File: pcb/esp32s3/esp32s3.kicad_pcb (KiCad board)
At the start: 2 copper layers, 64.5 x 64.5 mm, 82 parts, among them J1 USB_C_Receptacle_USB2.0_14P, J2 Battery, J3 GPS_ANT, Q1 DMG3414U, Q1_Xtal1 32.0MHz, SW1 BOOT, U1 ESP32-S3FN8, U2 AZ1117-3.3, U3 USBLC6-2SC6, U4 MCP73831-2-OT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

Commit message: pcb update!!!
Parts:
- added J4: LH128R-IG01, LH128R-IG01:LH128R-IG01, F.Cu at (159.7, 58.1)
- added Q2: DMG1012T, Package_TO_SOT_SMD:SOT-523, F.Cu at (157.4, 66.5)
- added R19: 10, Resistor_SMD:R_0402_1005Metric, F.Cu at (156.9, 60.0)
- added R20: 10K, Resistor_SMD:R_0402_1005Metric, F.Cu at (156.9, 61.9)
- added R21: 1K, Resistor_SMD:R_0402_1005Metric, F.Cu at (156.9, 63.9)
- C2: value 2p4 -> 2.4pF
- C4: value 2p7 -> 2.7pF
- C7, C8, C9: value 0.1uF -> 100nF
- L1: value 2n4 -> 2.4nH
- moved J1 14.9 mm to (129.5, 43.0), turned to 180 degrees
- moved U2 3.45 mm to (134.0, 62.0)
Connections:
- U1 pad 42: GP37 -> LCD_BL
- U1 pad 43: GP38 -> LCD_DC
- U1 pad 44: GP39 -> LCD_CS
- U1 pad 45: GP40 -> LCD_SCK
- U1 pad 47: GP41 -> LCD_SDA
- U1 pad 48: GP42 -> LCD_RST

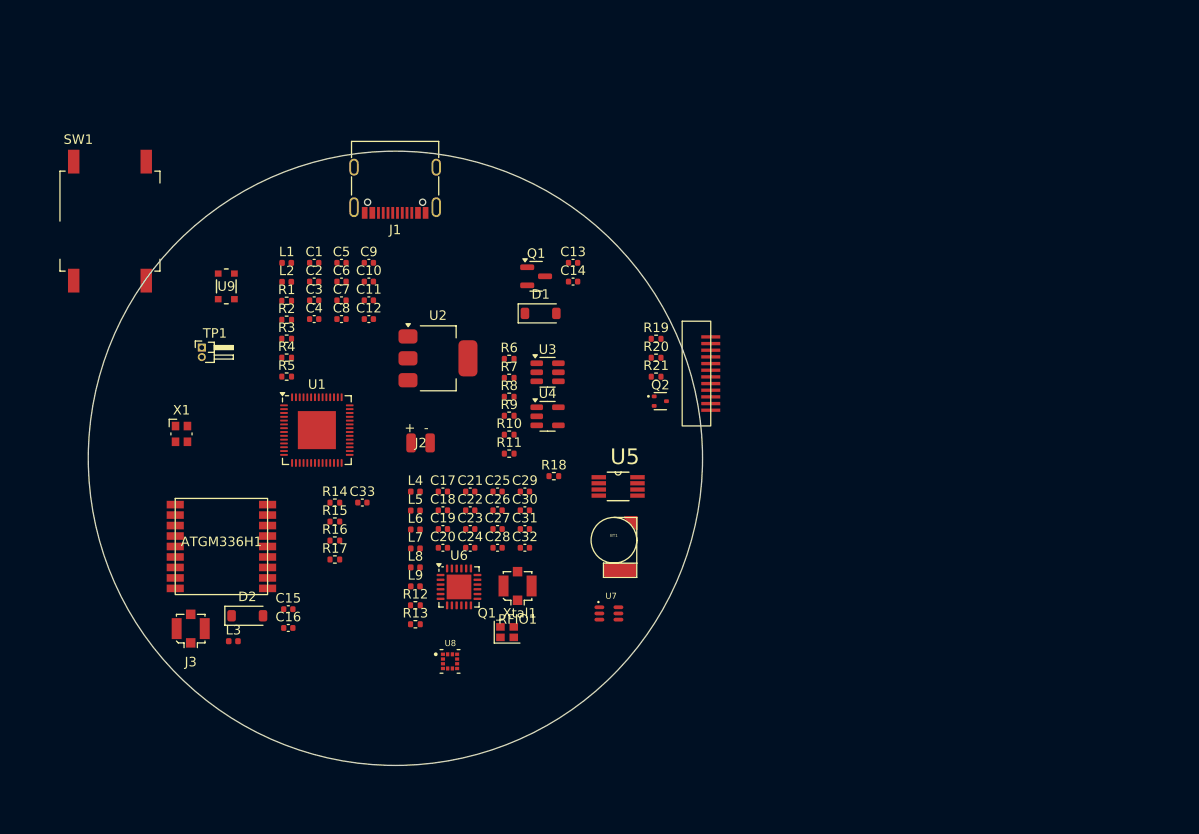
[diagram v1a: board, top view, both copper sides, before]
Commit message: Update PCB with new components and footprints
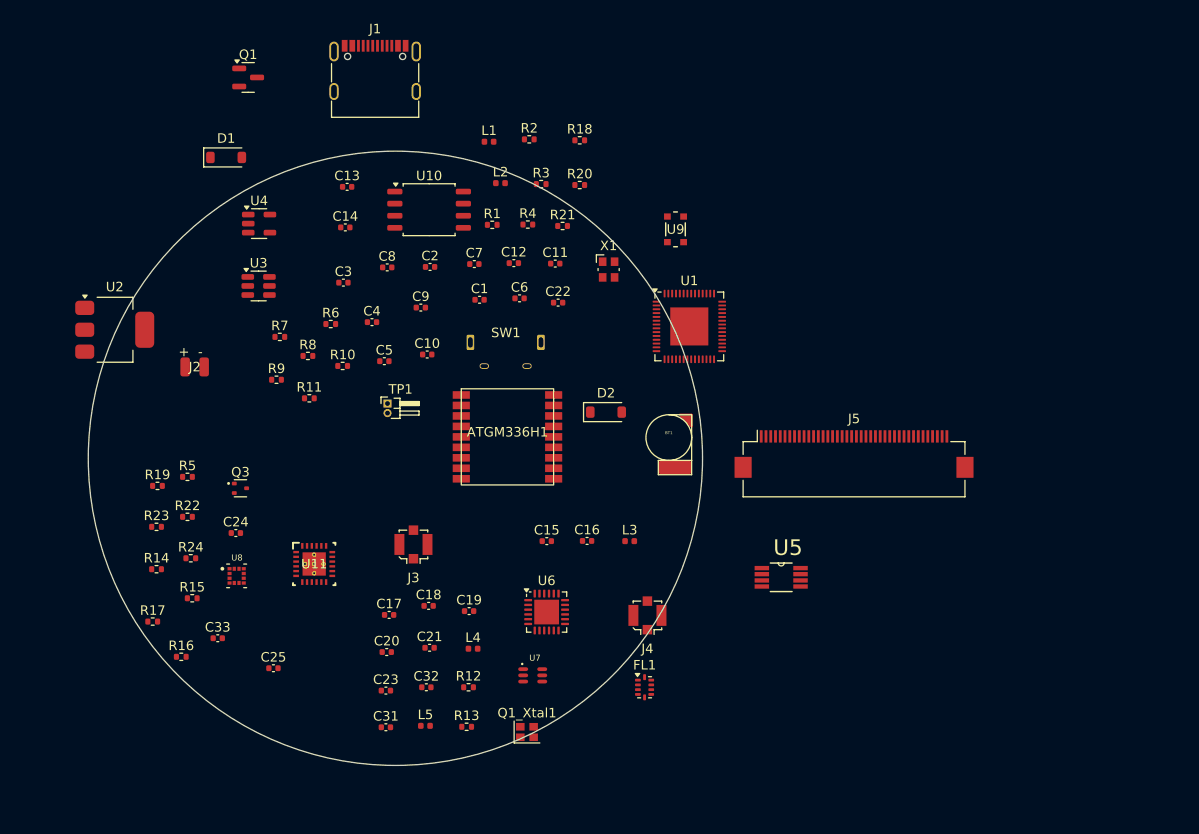
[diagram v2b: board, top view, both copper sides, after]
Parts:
- removed C26, C28: 3.3pF, Capacitor_SMD:C_0402_1005Metric
- removed C27, C30: 39pF, Capacitor_SMD:C_0402_1005Metric
- removed C29: 1.8pF, Capacitor_SMD:C_0402_1005Metric
- removed L6: 47nH, Inductor_SMD:L_0402_1005Metric
- removed L7: 2.5nH, Inductor_SMD:L_0402_1005Metric
- removed L8: 9.1nH, Inductor_SMD:L_0402_1005Metric
- removed L9: 4.7nH, Inductor_SMD:L_0402_1005Metric
- removed Q2: DMG1012T, Package_TO_SOT_SMD:SOT-523
- removed RFIO1: SMA, Connector_Coaxial:U.FL_Molex_MCRF_73412-0110_Vertical
- added FL1: 0900FM15K0039, RF_Converter:Balun_Johanson_0900FM15K0039, F.Cu at (155.7, 96.5)
- added J5: Conn_01x40_Socket, Connector_FFC-FPC:Hirose_FH12-40S-0.5SH_1x40-1MP_P0.50mm_Horizontal, F.Cu at (177.7, 72.0)
- added Q3: DMG1012T, Package_TO_SOT_SMD:SOT-523, F.Cu at (113.3, 75.7)
- added R22: 10K, Resistor_SMD:R_0402_1005Metric, F.Cu at (107.7, 78.7)
- added R23: 10, Resistor_SMD:R_0402_1005Metric, F.Cu at (104.4, 79.7)
- added R24: 5.1k, Resistor_SMD:R_0402_1005Metric, F.Cu at (108.0, 83.0)
- added U10: W25Q128JVS, Package_SO:SOIC-8_5.23x5.23mm_P1.27mm, F.Cu at (133.1, 46.4)
- added U11: TCA9539RGER, custom_comps:RGE0024B, F.Cu at (121.0, 83.6)
- ATGM336H1: footprint footprints:ATGM336H -> custom_comps:ATGM336H
- BT1: footprint footprints:MSR421R -> custom_comps:MSR421R
- C19: value 1.8pF -> 39pF
- C22: value 2.4pF -> 100nF
- C24: value 3pF -> 100nF
- C25: value 5.6pF -> 100nF
- J2: footprint footprints:2 Wire Pads -> custom_comps:2 Wire Pads
- J4: value LH128R-IG01 -> Conn_Coaxial; footprint LH128R-IG01:LH128R-IG01 -> Connector_Coaxial:U.FL_Molex_MCRF_73412-0110_Vertical
- L2: value 2n2 -> 2.2nH
- L5: value 15nH -> 47nH
- R19: value 10 -> 10K
- R2: value 5k1 -> 5.1k
- R20: value 10K -> 5.1k
- R21: value 1K -> 5.1k
- R5: value 10k -> 100
- SW1: footprint Button_Switch_SMD:SW_MEC_5GSH9 -> custom_comps:vert_button_6mm
- U1: value ESP32-S3FN8 -> ESP32-S3N8
- U5: footprint KiCAD Parts:SOP65P490X110-8N -> custom_comps:SOP65P490X110-8N
- U7: footprint KiCAD Parts:SOT65P215X110-6N -> custom_comps:SOT65P215X110-6N
- U8: footprint KiCAD Parts:PQFN50P200X200X100-12N -> custom_comps:PQFN50P200X200X100-12N
- U9: footprint 2450AT18D0100E:2450AT18D0100E_JOT -> custom_comps:2450AT18D0100E_JOT
- moved R19 54.6 mm to (104.5, 75.4)
- moved X1 48.1 mm to (151.9, 52.7)
- moved U9 47.6 mm to (158.9, 48.5)
- moved SW1 43.5 mm to (141.1, 60.3)
- moved D2 43.3 mm to (151.7, 67.7)
- moved L3 42.9 mm to (154.1, 81.2)
- moved U1 40.6 mm to (160.4, 58.6)
- moved D1 36.9 mm to (111.8, 40.9)
- moved Q1 36.8 mm to (114.1, 32.5)
- moved U4 36.4 mm to (115.2, 47.9)
- moved R18 35.4 mm to (148.9, 39.1)
- moved U2 34.1 mm to (100.0, 59.0)
- moved C16 32.7 mm to (149.7, 81.2)
- moved ATGM336H1 32.2 mm to (141.3, 70.2)
- moved R2 31.8 mm to (143.6, 39.0)
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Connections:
- net GP1 renamed BAT_V
- C19 pad 1: Net-(C19-Pad1) -> Net-(J4-In)
- C19 pad 2: GND -> Net-(U7-RFC)
- C22 pad 1: Net-(C19-Pad1) -> VDD_SPI
- C22 pad 2: Net-(U7-RF2) -> GND
- C24 pad 1: Net-(U6-RFO) -> VDD
- C24 pad 2: Net-(C24-Pad2) -> GND
- C25 pad 1: Net-(C24-Pad2) -> GND
- C25 pad 2: GND -> VDD
- J4 pad 1: GND -> Net-(J4-In)
- J4 pad 2: Net-(J4-LEDK) -> GND
- L5 pad 1: Net-(U6-RFI_N) -> Net-(U6-VR_PA)
- L5 pad 2: Net-(C19-Pad1) -> Net-(FL1-RFO)
- R13 pad 2: ANT_SW -> VDD
- R16 pad 2: XL_COMP_SDA -> SDA
- R17 pad 2: XL_COMP_SCL -> SCL
- R19 pad 1: Net-(J4-LEDK) -> LCD_CS
- R19 pad 2: Net-(Q2-D) -> VDD
- R20 pad 1: GND -> +3V3
- R20 pad 2: Net-(Q2-G) -> SCL
- R21 pad 1: LCD_BL -> +3V3
- R21 pad 2: Net-(Q2-G) -> SDA
- R5 pad 1: +3V3 -> LCD_PCLK
- R5 pad 2: Net-(U1-GPIO45) -> Net-(J5-Pin_12)
- U1 pad 10: GPS_RXD -> MOSI
- U1 pad 11: GPS_RESET -> SCK
- U1 pad 12: GPS_ON -> SCL
- U1 pad 13: XL_COMP_SCL -> SDA
- U1 pad 14: XL_COMP_SDA -> GPIO_RST
- U1 pad 15: INT_MAG -> GPIO_INT
- U1 pad 16: XL_INT0 -> LCD_DE
- U1 pad 17: XL_INT1 -> LCD_PCLK
- U1 pad 18: LoRa_MISO -> LCD_B1
- U1 pad 19: LoRa_MOSI -> LCD_B2
- U1 pad 21: unconnected-(U1-XTAL_32K_P-Pad21) -> LCD_HSYNC
- U1 pad 22: unconnected-(U1-XTAL_32K_N-Pad22) -> LCD_VSYNC
- U1 pad 23: LoRa_NSS -> LCD_B3
- U1 pad 24: LoRa_SCK -> LCD_B4
- U1 pad 27: LoRa_RST -> LCD_B5
- U1 pad 29: +3V3 -> VDD_SPI
- U1 pad 30: unconnected-(U1-SPIHD-Pad30) -> SPI_IO3
- U1 pad 31: unconnected-(U1-SPIWP-Pad31) -> SPI_IO2
- U1 pad 32: unconnected-(U1-SPICS0-Pad32) -> SPI_CS0
- U1 pad 33: unconnected-(U1-SPICLK-Pad33) -> SPI_CLK
- U1 pad 34: unconnected-(U1-SPIQ-Pad34) -> SPI_IO1
- U1 pad 35: unconnected-(U1-SPID-Pad35) -> SPI_IO0
- U1 pad 36: GP48 -> LCD_G5
- U1 pad 37: GP47 -> LCD_G4
- U1 pad 38: GP33 -> unconnected-(U1-GPIO33-Pad38)
- U1 pad 39: GP34 -> unconnected-(U1-GPIO34-Pad39)
- U1 pad 40: GP35 -> unconnected-(U1-GPIO35-Pad40)
- U1 pad 41: GP36 -> unconnected-(U1-GPIO36-Pad41)
- U1 pad 42: LCD_BL -> unconnected-(U1-GPIO37-Pad42)
- U1 pad 43: LCD_DC -> LCD_G3
- U1 pad 44: LCD_CS -> LCD_G2
- U1 pad 45: LCD_SCK -> LCD_G1
- U1 pad 47: LCD_SDA -> LCD_G0
- U1 pad 48: LCD_RST -> LCD_R5
- U1 pad 49: LoRa_DIO1 -> LCD_R4
- U1 pad 50: LoRa_BUSY -> LCD_R3
- U1 pad 51: Net-(U1-GPIO45) -> LCD_R2
- U1 pad 52: unconnected-(U1-GPIO46-Pad52) -> LCD_R1
- U1 pad 7: GP2 -> GPS_TXD
- U1 pad 8: unconnected-(U1-GPIO3-Pad8) -> GPS_RXD
- U1 pad 9: GPS_TXD -> MISO
- U4 pad 1: GP2 -> CHG_STAT
- U6 pad 16: LoRa_MISO -> MISO
- U6 pad 17: LoRa_MOSI -> MOSI
- U6 pad 21: GND -> Net-(FL1-RFI_P)
- U6 pad 22: Net-(U6-RFI_N) -> Net-(FL1-RFI_N)
- U6 pad 23: Net-(U6-RFO) -> Net-(FL1-RFO)
- U7 pad 3: Net-(U7-RF2) -> Net-(FL1-SW_RFO)

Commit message: pcb kinda almost done!
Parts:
- added R20: 5.1k, Resistor_SMD:R_0402_1005Metric, F.Cu at (180.2, 57.5)
- added R21: 5.1k, Resistor_SMD:R_0402_1005Metric, F.Cu at (180.4, 61.1)
- moved R19 69.3 mm to (173.8, 73.6)
- moved R2 62.6 mm to (112.9, 93.6), turned to 180 degrees
- moved TP1 62.2 mm to (189.0, 51.7)
- moved C24 62.2 mm to (173.1, 65.3)
- moved R10 62.2 mm to (184.3, 47.8)
- moved R11 62.2 mm to (180.8, 51.1)
- moved C25 62.2 mm to (177.0, 79.5)
- moved R1 60.5 mm to (200.1, 44.7)
- moved U9 58.9 mm to (130.1, 99.8), turned to -90 degrees
- moved FL1 58.8 mm to (209.6, 73.0)
- moved U7 58.8 mm to (197.8, 71.8)
- moved C17 58.8 mm to (182.8, 65.5)
- moved C18 58.8 mm to (186.9, 64.5)
- moved C19 58.8 mm to (191.2, 65.0)
- moved C20 58.8 mm to (182.5, 69.3)
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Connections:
- C25 pad 2: VDD -> +3V3
- C3 pad 1: Net-(C3-Pad1) -> GP0
- R13 pad 2: VDD -> +3V3
- R14 pad 2: unconnected-(R14-Pad2) -> /Accel & Magnetometer/CS_XL
- R15 pad 2: unconnected-(R15-Pad2) -> /Accel & Magnetometer/CS_MAG
- R2 pad 2: Net-(C3-Pad1) -> GP0
- SW1 pad 2: Net-(C3-Pad1) -> GP0
- U1 pad 10: MOSI -> LCD_B5
- U1 pad 11: SCK -> LCD_G0
- U1 pad 12: SCL -> LCD_G1
- U1 pad 13: SDA -> LCD_G2
- U1 pad 14: GPIO_RST -> LCD_G3
- U1 pad 15: GPIO_INT -> BAT_V
- U1 pad 16: LCD_DE -> LCD_G4
- U1 pad 17: LCD_PCLK -> LCD_G5
- U1 pad 18: LCD_B1 -> LCD_R1
- U1 pad 19: LCD_B2 -> LCD_R2
- U1 pad 21: LCD_HSYNC -> LCD_R3
- U1 pad 22: LCD_VSYNC -> LCD_R4
- U1 pad 23: LCD_B3 -> LCD_R5
- U1 pad 24: LCD_B4 -> GPIO_INT
- U1 pad 27: LCD_B5 -> GPIO_RST
- U1 pad 36: LCD_G5 -> SDA
- U1 pad 37: LCD_G4 -> SCL
- U1 pad 43: LCD_G3 -> MOSI
- U1 pad 44: LCD_G2 -> MISO
- U1 pad 45: LCD_G1 -> SCK
- U1 pad 47: LCD_G0 -> GPS_RXD
- U1 pad 48: LCD_R5 -> GPS_TXD
- U1 pad 49: LCD_R4 -> LCD_PCLK
- U1 pad 50: LCD_R3 -> LCD_DE
- U1 pad 51: LCD_R2 -> LCD_VSYNC
- U1 pad 52: LCD_R1 -> LCD_HSYNC
- U1 pad 6: BAT_V -> LCD_B1
- U1 pad 7: GPS_TXD -> LCD_B2
- U1 pad 8: GPS_RXD -> LCD_B3
- U1 pad 9: MISO -> LCD_B4
- U11 pad 19: GPIO_SCL -> SCL
- U11 pad 20: GPIO_SDA -> SDA
- U11 pad 21: VDD -> +3V3
- U3 pad 1: USB_D- -> USB_D+
- U3 pad 3: USB_D+ -> USB_D-
- U3 pad 4: Net-(J1-D+-PadA6) -> Net-(J1-D--PadA7)
- U3 pad 6: Net-(J1-D--PadA7) -> Net-(J1-D+-PadA6)
- U8 pad 1: unconnected-(U8-SCL/SPC-Pad1) -> SDA
- U8 pad 2: unconnected-(U8-CS_XL-Pad2) -> /Accel & Magnetometer/CS_XL
- U8 pad 3: unconnected-(U8-CS_MAG-Pad3) -> /Accel & Magnetometer/CS_MAG
- U8 pad 4: unconnected-(U8-SDA/SDI/SDO-Pad4) -> SCL
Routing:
- net SDA: track 0.00 -> 40.6 mm, vias 0 -> 4
- net GP0: track 0.00 -> 40.4 mm, vias 0 -> 2
- net GPS_ON: track 0.00 -> 38.4 mm, vias 0 -> 2
- net +3V3: track 0.00 -> 38.3 mm, vias 0 -> 13
- net SCL: track 0.00 -> 38.1 mm, vias 0 -> 4
- net VBUS: track 0.00 -> 36.2 mm
- net LCD_CS: track 0.00 -> 26.8 mm, vias 0 -> 2
- net LCD_RST: track 0.00 -> 24.7 mm, vias 0 -> 2
- net GPS_RXD: track 0.00 -> 24.3 mm, vias 0 -> 2
- net GPS_TXD: track 0.00 -> 24.0 mm, vias 0 -> 2
- net USB_D-: track 0.00 -> 23.8 mm
- net USB_D+: track 0.00 -> 23.8 mm
- net VCC: track 0.00 -> 22.7 mm, vias 0 -> 2
- net LNA_IN: track 0.00 -> 22.6 mm
- net INT_MAG: track 0.00 -> 22.5 mm, vias 0 -> 2
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- added copper zone on In2.Cu, net +3V3
- added copper zone on B.Cu, net GP0
- added copper zone on F.Cu, net GP0
- added copper zone on In1.Cu, net GP0
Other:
- board size 64.5 x 64.5 mm -> 59.8 x 58.9 mm
- copper layers 2 -> 4

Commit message: LORA
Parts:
- removed U7: PE4259, custom_comps:SOT65P215X110-6N
- added U12: BGS12SN6E6327XTSA1, BGS12SN6:TSNP-6-2&slash_-8_INF, F.Cu at (148.9, 79.6)
- L4: footprint Inductor_SMD:L_0402_1005Metric -> Inductor_SMD:L_0805_2012Metric
- moved J4 64.4 mm to (148.9, 86.2), turned to 180 degrees
- moved FL1 60.4 mm to (149.2, 74.7), turned to -90 degrees
- moved C19 45.5 mm to (148.9, 82.0), turned to 90 degrees
- moved R13 44.8 mm to (146.1, 78.7), turned to 180 degrees
- moved L4 41.7 mm to (150.2, 63.8)
- moved C32 41.1 mm to (146.1, 79.8), turned to 180 degrees
- moved R12 40.1 mm to (151.4, 78.8)
- moved C18 39.5 mm to (147.4, 65.1), turned to 180 degrees
- moved C21 36.6 mm to (150.6, 65.5), turned to 180 degrees
- moved L5 36.0 mm to (150.8, 72.6), turned to 180 degrees
- moved C31 31.1 mm to (151.4, 79.8)
- moved C17 30.8 mm to (152.5, 71.0), turned to -90 degrees
- moved C20 30.3 mm to (152.7, 74.8)
- moved C23 29.7 mm to (152.7, 73.7)
- moved U6 11.8 mm to (148.8, 68.8), turned to 180 degrees
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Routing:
- net GND: track 15.8 -> 39.2 mm, vias 2 -> 151
- net ANT_SW_CTRL: track 0.00 -> 16.5 mm, vias 0 -> 2
- net Net-(U6-XTA): track 0.00 -> 6.01 mm, vias 0 -> 2
- net Net-(FL1-SW_RFI): track 0.00 -> 4.17 mm
- net Net-(FL1-SW_RFO): track 0.00 -> 4.09 mm
- net Net-(FL1-RFO): track 0.00 -> 3.69 mm
- net Net-(U6-XTB): track 0.00 -> 3.51 mm, vias 0 -> 2
- net Net-(FL1-RFI_P): track 0.00 -> 3.23 mm
- net Net-(FL1-RFI_N): track 0.00 -> 3.23 mm
- net Net-(U12-VDD): track 0.00 -> 3.03 mm
- net +3V3: track 38.3 -> 41.3 mm, vias 13 -> 18
- net Net-(J4-In): track 0.00 -> 2.22 mm
- net Net-(U12-RFIN): track 0.00 -> 1.91 mm
- net MOSI: track 0.00 -> 1.88 mm, vias 0 -> 1
- net LoRa_NSS: track 0.00 -> 1.87 mm, vias 0 -> 1
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- added copper zone on F.Cu, net +3V3
- added copper zone on B.Cu, net GND
- added copper zone on F.Cu, net GND
- added copper zone on In1.Cu, net GND
- added copper zone on F.Cu, net Net-(U6-DCC_SW)
- added copper zone on F.Cu, net Net-(U6-VREG)
- added copper zone on F.Cu, net Net-(U6-VR_PA)
- removed copper zone on B.Cu, net GP0
- removed copper zone on F.Cu, net GP0
- removed copper zone on In1.Cu, net GP0

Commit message: finishing touches
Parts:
- removed R20 (x2), R21 (x2): 5.1k, Resistor_SMD:R_0402_1005Metric
- removed TP1: Reset, Connector_PinHeader_1.00mm:PinHeader_1x02_P1.00mm_Horizontal
- added SW2: PTS815 SJM 250 SMTR LFS, custom_comps:SW4_PTS815 SJM 250 SMTR LFS_CNK, F.Cu at (104.5, 72.3)
- U12: footprint BGS12SN6:TSNP-6-2&slash_-8_INF -> custom_comps:TSNP-6-2&slash_-8_INF
- moved R1 96.8 mm to (106.3, 68.4)
- moved C24 44.9 mm to (133.1, 85.8)
- moved R10 43.6 mm to (142.0, 58.4), turned to 90 degrees
- moved R19 40.8 mm to (133.1, 87.1), turned to 180 degrees
- moved R11 40.8 mm to (140.7, 58.4), turned to -90 degrees
- moved C25 26.5 mm to (144.9, 62.8), turned to -90 degrees
- moved C3 8.93 mm to (113.1, 85.9), turned to -90 degrees
- moved R2 7.87 mm to (114.4, 85.9), turned to 90 degrees
- moved C4 2.19 mm to (130.9, 93.0)
- moved C2 1.53 mm to (130.9, 96.4)
- moved R7 0.74 mm to (133.8, 51.4)
- moved L1 0.70 mm to (131.4, 94.7)
- moved R17 0.30 mm to (135.6, 90.9)
- moved R14 0.30 mm to (135.6, 88.3)
- moved R15 0.30 mm to (135.6, 89.6)
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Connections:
- net LoRa_DIO3 renamed /LoRa/DIO3
- C24 pad 1: VDD -> +3V3
- J5 pad 1: VDD -> +3V3
- J5 pad 5: VDD -> +3V3
- J5 pad 9: /LCD/LCD_MOSI -> MOSI
- R1 pad 1: +3V3 -> CHIP_PU
- R1 pad 2: Net-(R1-Pad2) -> +3V3
- R19 pad 2: VDD -> +3V3
- U11 pad 5: LCD_DE -> /IO Expander/GPIO_P04
- U6 pad 18: LoRa_SCK -> SCK
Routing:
- net MOSI: track 1.88 -> 82.7 mm, vias 1 -> 5
- net MISO: track 1.77 -> 70.5 mm, vias 1 -> 4
- net LoRa_BUSY: track 1.84 -> 65.5 mm, vias 1 -> 2
- net LoRa_DIO1: track 1.24 -> 63.2 mm, vias 1 -> 2
- net SCK: track 0.00 -> 60.1 mm, vias 0 -> 4
- net LoRa_NSS: track 1.87 -> 61.2 mm, vias 1 -> 2
- net LoRa_RST: track 1.78 -> 60.7 mm, vias 1 -> 2
- net CHG_STAT: track 0.00 -> 51.1 mm, vias 0 -> 4
- net CHIP_PU: track 0.00 -> 33.2 mm, vias 0 -> 2
- net BAT_V: track 0.00 -> 25.9 mm, vias 0 -> 2
- net Net-(J5-Pin_2): track 0.00 -> 18.8 mm, vias 0 -> 2
- net +3V3: track 41.3 -> 58.2 mm, vias 18 -> 24
- net GND: track 39.2 -> 54.0 mm, vias 151 -> 359
- net LCD_CS: track 26.8 -> 38.0 mm, vias 2 -> 3
- net +BATT: track 8.96 -> 13.4 mm
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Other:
- board size 59.8 x 58.9 mm -> 59.7 x 58.9 mm
- board text added: ": 3"
- board text added: "Festival Tracker v0.1 Big Z and Lil T Productions"
